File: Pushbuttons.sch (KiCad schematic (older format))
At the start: 19 parts, among them SW1301 Time, SW1302 Date, SW1303 Alarm, SW1304 Display, SW1305 Brightness, SW1306 Select, U1301 MAX6818

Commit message: Resolved an issue with the field names of resistors on anode and grid driver sheets
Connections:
- wire segments 63 -> 82
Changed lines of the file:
@@
 	3240 1770 3240 1810
 Wire Wire Line
-	3240 1770 3880 1770
-Wire Wire Line
-	3560 1730 3560 1810
+	3240 1770 3560 1770
+Wire Wire Line
+	3560 1730 3560 1770
 Wire Wire Line
 	3880 2150 3880 2110
@@
 	3240 2150 3240 2110
 Wire Wire Line
-	3240 2150 3880 2150
-Wire Wire Line
-	3560 2110 3560 2190
+	3240 2150 3560 2150
+Wire Wire Line
+	3560 2110 3560 2150
 Wire Wire Line
 	2460 3390 3970 3390
@@
 ~Encoder_B
 Wire Wire Line
-	4770 3090 7040 3090
-Wire Wire Line
-	4770 3190 7040 3190
-Wire Wire Line
-	4770 3290 7040 3290
-Wire Wire Line
-	4770 3390 7040 3390
-Wire Wire Line
-	4770 3490 7040 3490
-Wire Wire Line
-	4770 3590 7040 3590
-Wire Wire Line
-	4770 3690 7040 3690
-Wire Wire Line
-	4770 3790 7040 3790
+	4770 3090 5540 3090
+Wire Wire Line
+	4770 3190 5720 3190
+Wire Wire Line
+	4770 3290 5900 3290
+Wire Wire Line
+	4770 3390 6080 3390
+Wire Wire Line
+	4770 3490 6260 3490
+Wire Wire Line
+	4770 3590 6440 3590
+Wire Wire Line
+	4770 3690 6620 3690
+Wire Wire Line
+	4770 3790 6800 3790
 $Comp
 L Custom-Library:+3.3V #PWR1313
@@
 	6170 2470 6170 2430
 Wire Wire Line
-	5540 2470 6800 2470
+	5540 2470 5720 2470
 Wire Wire Line
 	6080 2470 6080 2510
@@
 Connection ~ 6800 3790
 NoConn ~ 4770 2940
+Wire Wire Line
+	3560 1770 3880 1770
+Wire Wire Line
+	3560 1770 3560 1810
+Wire Wire Line
+	3560 2150 3880 2150
+Wire Wire Line
+	3560 2150 3560 2190
+Wire Wire Line
+	6080 2470 6170 2470
+Wire Wire Line
+	5900 2470 6080 2470
+Wire Wire Line
+	6170 2470 6260 2470
+Wire Wire Line
+	6260 2470 6440 2470
+Wire Wire Line
+	6440 2470 6620 2470
+Wire Wire Line
+	5720 2470 5900 2470
+Wire Wire Line
+	6620 2470 6800 2470
+Wire Wire Line
+	5540 3090 7040 3090
+Wire Wire Line
+	5720 3190 7040 3190
+Wire Wire Line
+	5900 3290 7040 3290
+Wire Wire Line
+	6080 3390 7040 3390
+Wire Wire Line
+	6260 3490 7040 3490
+Wire Wire Line
+	6440 3590 7040 3590
+Wire Wire Line
+	6620 3690 7040 3690
+Wire Wire Line
+	6800 3790 7040 3790
 $EndSCHEMATC

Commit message: Altered encoder circuit to use little logic to simplify firmware, resized active low signals to it on micro better, updated PDF
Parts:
- removed R1308, R1309: 10k, Resistors_SMD:R_0603, symbol VFD_Clock-rescue:Res_Custom
- added C? (x2): 2.2uF, symbol Custom-Library:C_Custom
- added C? (x2): 0.1uF, Capacitors_SMD:C_0603, symbol Custom-Library:C_Custom
- added R? (x5): 10k, Resistors_SMD:R_0603, symbol VFD_Clock-rescue:Res_Custom
- added R? (x2): 1k, Resistors_SMD:R_0603, symbol Device:R
- added U? (x2): 74LVC2G14, symbol Custom_Library:74LVC2G14_Power
- added U?: 74LVC1G79, symbol Custom_Library:74LVC1G79_Power
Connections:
- net labels added: Encoder_DIR, Encoder_STEP
- net labels removed: ~Encoder_A, ~Encoder_B
- wire segments 82 -> 97

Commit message: Annotated all components, finished assigning footprints, netlist generated
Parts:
- C1304, C1305: renamed from C?; footprint (none) -> Capacitors_SMD:C_0805
- U1302: renamed from U?; footprint (none) -> TO_SOT_Packages_SMD:SOT-363_SC-70-6; Digi-Key PN (none) -> 296-13011-1-ND
- U1303: renamed from U?; footprint (none) -> TO_SOT_Packages_SMD:SOT-353_SC-70-5; Digi-Key PN (none) -> 296-47671-1-ND
- gave numbers to parts that had none: 9
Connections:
- no-connect marks 1 -> 5

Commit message: Switched to QFN micro, various footprint fixes, layed a a few more sheets out, changed puchbutton debouncers
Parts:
- removed C1301: 1nF, Capacitors_SMD:C_0603, symbol Custom-Library:C_Custom
- removed R1307: 10k, Resistors_SMD:R_0603, symbol VFD_Clock-rescue:Res_Custom
- removed U1301: MAX6818, Housings_SSOP:SSOP-20_5.3x7.2mm_Pitch0.65mm, symbol Custom-Library:MAX6818
- added C1303, C1308, C1309, C1310: 0.1uF, Capacitors_SMD:C_0603, symbol Custom-Library:C_Custom
- added U1301, U1304, U1305, U1306, U1307, U1308: MAX6816, TO_SOT_Packages_SMD:SOT-143, symbol Custom_Library:MAX6816
- C1302: value 10nF -> 0.1uF
- R1301, R1302, R1303, R1304, R1305, R1306: Wattage 1/16W -> 1/10W; display_footprint 0402 -> 0603
- renumbered C1303 to C1301
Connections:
- wire segments 97 -> 53
- no-connect marks 5 -> 0

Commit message: Added a bunch of Digi-Key PN's
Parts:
- C1301, C1302, C1303, C1306, C1307, C1308, C1309, C1310: Digi-Key PN (none) -> 399-6856-1-ND
- R1301, R1302, R1303, R1304, R1305, R1306, R1312, R1313, R1314: Digi-Key PN (none) -> 541-10.0KHCT-ND
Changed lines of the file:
@@
 F 5 "50V" H 2540 1730 50  0000 R CNN "Voltage"
 F 6 "X7R" H 2540 1630 50  0000 R CNN "Dielectric"
+F 7 "399-6856-1-ND" H 0   0   50  0001 C CNN "Digi-Key PN"
 	1    2690 1730
 	-1   0    0    -1
@@
 F 5 "1/10W" V 3160 5440 50  0001 C CNN "Wattage"
 F 6 "0603" V 3080 5440 50  0001 C CNN "display_footprint"
+F 7 "" H 0   0   50  0001 C CNN "Digi-Key PN"
 	1    3260 5440
 	0    -1   -1   0
@@
 F 5 "1/10W" V 3160 5640 50  0001 C CNN "Wattage"
 F 6 "0603" V 3080 5640 50  0001 C CNN "display_footprint"
+F 7 "" H 0   0   50  0001 C CNN "Digi-Key PN"
 	1    3260 5640
 	0    -1   -1   0
@@
 F 5 "50V" H 5300 6360 50  0000 R CNN "Voltage"
 F 6 "X7R" H 5300 6260 50  0000 R CNN "Dielectric"
+F 7 "399-6856-1-ND" H 0   0   50  0001 C CNN "Digi-Key PN"
 	1    5450 6360
 	-1   0    0    -1
@@
 F 5 "1%" H 6740 6130 50  0000 L CNN "Tolerance"
 F 6 "1/10W" H 6730 6200 50  0000 L CNN "Wattage"
+F 7 "541-10.0KHCT-ND" H 0   0   50  0001 C CNN "Digi-Key PN"
 	1    6670 6150
 	-1   0    0    -1
@@
 F 5 "1%" H 7370 6130 50  0000 L CNN "Tolerance"
 F 6 "1/10W" H 7360 6200 50  0000 L CNN "Wattage"
+F 7 "541-10.0KHCT-ND" H 0   0   50  0001 C CNN "Digi-Key PN"
 	1    7300 6150
 	-1   0    0    -1
@@
 F 5 "50V" H 7910 6330 50  0000 R CNN "Voltage"
 F 6 "X7R" H 7910 6230 50  0000 R CNN "Dielectric"
+F 7 "399-6856-1-ND" H 0   0   50  0001 C CNN "Digi-Key PN"
 	1    8060 6330
 	-1   0    0    -1
@@
 F 5 "1%" H 9360 5830 50  0000 L CNN "Tolerance"
 F 6 "1/10W" H 9350 5900 50  0000 L CNN "Wattage"
+F 7 "541-10.0KHCT-ND" H 0   0   50  0001 C CNN "Digi-Key PN"
 	1    9290 5850
 	-1   0    0    -1
@@
 F 5 "1%" H 3950 1050 50  0000 L CNN "Tolerance"
 F 6 "1/10W" H 3940 1120 50  0000 L CNN "Wattage"
+F 7 "541-10.0KHCT-ND" H 0   0   50  0001 C CNN "Digi-Key PN"
 	1    3880 1070
 	1    0    0    -1
@@
 F 5 "50V" H 5540 1730 50  0000 R CNN "Voltage"
 F 6 "X7R" H 5540 1630 50  0000 R CNN "Dielectric"
+F 7 "399-6856-1-ND" H 0   0   50  0001 C CNN "Digi-Key PN"
 	1    5690 1730
 	-1   0    0    -1
@@
 F 5 "1%" H 6950 1050 50  0000 L CNN "Tolerance"
 F 6 "1/10W" H 6940 1120 50  0000 L CNN "Wattage"
+F 7 "541-10.0KHCT-ND" H 0   0   50  0001 C CNN "Digi-Key PN"
 	1    6880 1070
 	1    0    0    -1
@@
 F 5 "50V" H 2540 2980 50  0000 R CNN "Voltage"
 F 6 "X7R" H 2540 2880 50  0000 R CNN "Dielectric"
+F 7 "399-6856-1-ND" H 0   0   50  0001 C CNN "Digi-Key PN"
 	1    2690 2980
 	-1   0    0    -1
@@
 F 5 "1%" H 3950 2300 50  0000 L CNN "Tolerance"
 F 6 "1/10W" H 3940 2370 50  0000 L CNN "Wattage"
+F 7 "541-10.0KHCT-ND" H 0   0   50  0001 C CNN "Digi-Key PN"
 	1    3880 2320
 	1    0    0    -1
@@
 F 5 "50V" H 5540 2980 50  0000 R CNN "Voltage"
 F 6 "X7R" H 5540 2880 50  0000 R CNN "Dielectric"
+F 7 "399-6856-1-ND" H 0   0   50  0001 C CNN "Digi-Key PN"
 	1    5690 2980
 	-1   0    0    -1
@@
 F 5 "1%" H 6950 2300 50  0000 L CNN "Tolerance"
 F 6 "1/10W" H 6940 2370 50  0000 L CNN "Wattage"
+F 7 "541-10.0KHCT-ND" H 0   0   50  0001 C CNN "Digi-Key PN"
 	1    6880 2320
 	1    0    0    -1
@@
 F 5 "50V" H 2540 4230 50  0000 R CNN "Voltage"
 F 6 "X7R" H 2540 4130 50  0000 R CNN "Dielectric"
+F 7 "399-6856-1-ND" H 0   0   50  0001 C CNN "Digi-Key PN"
 	1    2690 4230
 	-1   0    0    -1
@@
 F 5 "1%" H 3950 3550 50  0000 L CNN "Tolerance"
 F 6 "1/10W" H 3940 3620 50  0000 L CNN "Wattage"
+F 7 "541-10.0KHCT-ND" H 0   0   50  0001 C CNN "Digi-Key PN"
 	1    3880 3570
 	1    0    0    -1
@@
 F 5 "50V" H 5540 4230 50  0000 R CNN "Voltage"
 F 6 "X7R" H 5540 4130 50  0000 R CNN "Dielectric"
+F 7 "399-6856-1-ND" H 0   0   50  0001 C CNN "Digi-Key PN"
 	1    5690 4230
 	-1   0    0    -1
@@
 F 5 "1%" H 6950 3550 50  0000 L CNN "Tolerance"
 F 6 "1/10W" H 6940 3620 50  0000 L CNN "Wattage"
+F 7 "541-10.0KHCT-ND" H 0   0   50  0001 C CNN "Digi-Key PN"
 	1    6880 3570
 	1    0    0    -1

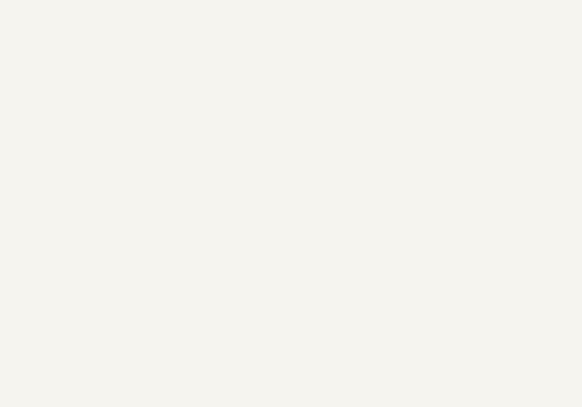
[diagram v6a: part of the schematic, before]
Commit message: Arranged more components on PCB, cleaned up schematic, added page titles, finished finding DigiKey PN's
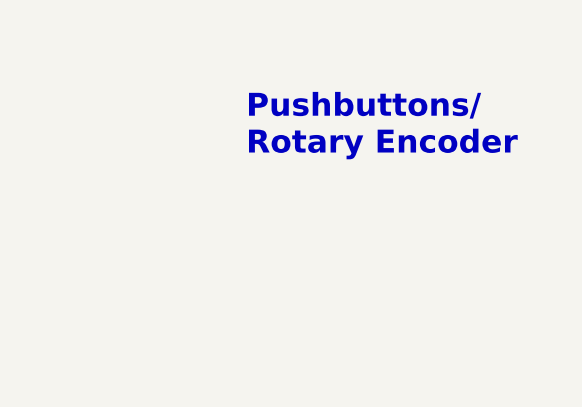
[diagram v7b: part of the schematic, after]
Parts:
- R1301, R1302, R1303, R1304, R1305, R1306, R1312, R1313, R1314: Digi-Key PN 541-10.0KHCT-ND -> P10.0KHCT-ND
- R1308, R1309: Digi-Key PN (none) -> P10.0KHCT-ND; Wattage 1/16W -> 1/10W; display_footprint 0402 -> 0603
- R1310, R1311: Digi-Key PN (none) -> RMCF0603FT1K00CT-ND
- SW1301, SW1302, SW1303, SW1304, SW1305: Digi-Key PN (none) -> 450-1650-ND
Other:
- note added: "Pushbuttons/\nRotary Encoder"
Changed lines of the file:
@@
 F 2 "Buttons_Switches_THT:SW_PUSH_6mm" H 2520 1470 50  0001 C CNN
 F 3 "" H 2520 1470 50  0001 C CNN
+F 4 "450-1650-ND" H 0   0   50  0001 C CNN "Digi-Key PN"
 	1    2520 1270
 	1    0    0    -1
@@
 F 2 "Buttons_Switches_THT:SW_PUSH_6mm" H 5520 1470 50  0001 C CNN
 F 3 "" H 5520 1470 50  0001 C CNN
+F 4 "450-1650-ND" H 0   0   50  0001 C CNN "Digi-Key PN"
 	1    5520 1270
 	1    0    0    -1
@@
 F 2 "Buttons_Switches_THT:SW_PUSH_6mm" H 2520 2720 50  0001 C CNN
 F 3 "" H 2520 2720 50  0001 C CNN
+F 4 "450-1650-ND" H 0   0   50  0001 C CNN "Digi-Key PN"
 	1    2520 2520
 	1    0    0    -1
@@
 F 2 "Buttons_Switches_THT:SW_PUSH_6mm" H 5520 2720 50  0001 C CNN
 F 3 "" H 5520 2720 50  0001 C CNN
+F 4 "450-1650-ND" H 0   0   50  0001 C CNN "Digi-Key PN"
 	1    5520 2520
 	1    0    0    -1
@@
 F 2 "Buttons_Switches_THT:SW_PUSH_6mm" H 5520 3970 50  0001 C CNN
 F 3 "" H 5520 3970 50  0001 C CNN
+F 4 "450-1650-ND" H 0   0   50  0001 C CNN "Digi-Key PN"
 	1    5520 3770
 	1    0    0    -1
@@
 F 2 "Resistors_SMD:R_0603" H 2660 5110 50  0001 C CNN
 F 3 "" H 2660 5110 50  0001 C CNN
-F 4 "0402" V 2760 5110 50  0001 C CNN "display_footprint"
+F 4 "0603" V 2760 5110 50  0001 C CNN "display_footprint"
 F 5 "1%" V 2860 5110 50  0001 C CNN "Tolerance"
-F 6 "1/16W" V 2960 5110 50  0001 C CNN "Wattage"
+F 6 "1/10W" V 2960 5110 50  0001 C CNN "Wattage"
+F 7 "P10.0KHCT-ND" H 0   0   50  0001 C CNN "Digi-Key PN"
 	1    2660 5110
 	1    0    0    -1
@@
 F 2 "Resistors_SMD:R_0603" H 2840 5110 50  0001 C CNN
 F 3 "" H 2840 5110 50  0001 C CNN
-F 4 "0402" V 2940 5110 50  0001 C CNN "display_footprint"
+F 4 "0603" V 2940 5110 50  0001 C CNN "display_footprint"
 F 5 "1%" V 3040 5110 50  0001 C CNN "Tolerance"
-F 6 "1/16W" V 3140 5110 50  0001 C CNN "Wattage"
+F 6 "1/10W" V 3140 5110 50  0001 C CNN "Wattage"
+F 7 "P10.0KHCT-ND" H 0   0   50  0001 C CNN "Digi-Key PN"
 	1    2840 5110
 	1    0    0    -1
@@
 F 5 "1/10W" V 3160 5440 50  0001 C CNN "Wattage"
 F 6 "0603" V 3080 5440 50  0001 C CNN "display_footprint"
-F 7 "" H 0   0   50  0001 C CNN "Digi-Key PN"
+F 7 "RMCF0603FT1K00CT-ND" H 0   0   50  0001 C CNN "Digi-Key PN"
 	1    3260 5440
 	0    -1   -1   0
@@
 F 5 "1/10W" V 3160 5640 50  0001 C CNN "Wattage"
 F 6 "0603" V 3080 5640 50  0001 C CNN "display_footprint"
-F 7 "" H 0   0   50  0001 C CNN "Digi-Key PN"
+F 7 "RMCF0603FT1K00CT-ND" H 0   0   50  0001 C CNN "Digi-Key PN"
 	1    3260 5640
 	0    -1   -1   0
@@
 U 1 1 5B56624B
 P 8280 5630
-F 0 "U1303" H 8180 5830 50  0000 R CNN
+F 0 "U1303" H 8410 5830 50  0000 L CNN
 F 1 "74LVC1G79" H 8620 5400 50  0000 C CNN
 F 2 "TO_SOT_Packages_SMD:SOT-353_SC-70-5" H 8280 5630 50  0001 C CNN
@@
 F 5 "1%" H 6740 6130 50  0000 L CNN "Tolerance"
 F 6 "1/10W" H 6730 6200 50  0000 L CNN "Wattage"
-F 7 "541-10.0KHCT-ND" H 0   0   50  0001 C CNN "Digi-Key PN"
+F 7 "P10.0KHCT-ND" H 0   0   50  0001 C CNN "Digi-Key PN"
 	1    6670 6150
 	-1   0    0    -1
@@
 F 5 "1%" H 7370 6130 50  0000 L CNN "Tolerance"
 F 6 "1/10W" H 7360 6200 50  0000 L CNN "Wattage"
-F 7 "541-10.0KHCT-ND" H 0   0   50  0001 C CNN "Digi-Key PN"
+F 7 "P10.0KHCT-ND" H 0   0   50  0001 C CNN "Digi-Key PN"
 	1    7300 6150
 	-1   0    0    -1
@@
 F 5 "1%" H 9360 5830 50  0000 L CNN "Tolerance"
 F 6 "1/10W" H 9350 5900 50  0000 L CNN "Wattage"
-F 7 "541-10.0KHCT-ND" H 0   0   50  0001 C CNN "Digi-Key PN"
+F 7 "P10.0KHCT-ND" H 0   0   50  0001 C CNN "Digi-Key PN"
 	1    9290 5850
 	-1   0    0    -1
@@
 F 5 "1%" H 3950 1050 50  0000 L CNN "Tolerance"
 F 6 "1/10W" H 3940 1120 50  0000 L CNN "Wattage"
-F 7 "541-10.0KHCT-ND" H 0   0   50  0001 C CNN "Digi-Key PN"
+F 7 "P10.0KHCT-ND" H 0   0   50  0001 C CNN "Digi-Key PN"
 	1    3880 1070
 	1    0    0    -1
@@
 F 5 "1%" H 6950 1050 50  0000 L CNN "Tolerance"
 F 6 "1/10W" H 6940 1120 50  0000 L CNN "Wattage"
-F 7 "541-10.0KHCT-ND" H 0   0   50  0001 C CNN "Digi-Key PN"
+F 7 "P10.0KHCT-ND" H 0   0   50  0001 C CNN "Digi-Key PN"
 	1    6880 1070
 	1    0    0    -1
@@
 F 5 "1%" H 3950 2300 50  0000 L CNN "Tolerance"
 F 6 "1/10W" H 3940 2370 50  0000 L CNN "Wattage"
-F 7 "541-10.0KHCT-ND" H 0   0   50  0001 C CNN "Digi-Key PN"
+F 7 "P10.0KHCT-ND" H 0   0   50  0001 C CNN "Digi-Key PN"
 	1    3880 2320
 	1    0    0    -1
@@
 F 5 "1%" H 6950 2300 50  0000 L CNN "Tolerance"
 F 6 "1/10W" H 6940 2370 50  0000 L CNN "Wattage"
-F 7 "541-10.0KHCT-ND" H 0   0   50  0001 C CNN "Digi-Key PN"
+F 7 "P10.0KHCT-ND" H 0   0   50  0001 C CNN "Digi-Key PN"
 	1    6880 2320
 	1    0    0    -1
@@
 F 5 "1%" H 3950 3550 50  0000 L CNN "Tolerance"
 F 6 "1/10W" H 3940 3620 50  0000 L CNN "Wattage"
-F 7 "541-10.0KHCT-ND" H 0   0   50  0001 C CNN "Digi-Key PN"
+F 7 "P10.0KHCT-ND" H 0   0   50  0001 C CNN "Digi-Key PN"
 	1    3880 3570
 	1    0    0    -1
@@
 F 5 "1%" H 6950 3550 50  0000 L CNN "Tolerance"
 F 6 "1/10W" H 6940 3620 50  0000 L CNN "Wattage"
-F 7 "541-10.0KHCT-ND" H 0   0   50  0001 C CNN "Digi-Key PN"
+F 7 "P10.0KHCT-ND" H 0   0   50  0001 C CNN "Digi-Key PN"
 	1    6880 3570
 	1    0    0    -1
@@
 	7520 3770 6880 3770
 Connection ~ 6880 3770
+Text Notes 9010 1090 0    100  ~ 20
+Pushbuttons/\nRotary Encoder
 $EndSCHEMATC

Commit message: Placed VAN power supply and asociated circuits
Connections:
- wire segments 53 -> 54
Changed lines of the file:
@@
 L power:GND #PWR01301
 U 1 1 5A4D2A4C
-P 1910 5640
-F 0 "#PWR01301" H 1910 5390 50  0001 C CNN
-F 1 "GND" H 1910 5490 50  0000 C CNN
-F 2 "" H 1910 5640 50  0001 C CNN
-F 3 "" H 1910 5640 50  0001 C CNN
-	1    1910 5640
+P 1800 5440
+F 0 "#PWR01301" H 1800 5190 50  0001 C CNN
+F 1 "GND" H 1800 5290 50  0000 C CNN
+F 2 "" H 1800 5440 50  0001 C CNN
+F 3 "" H 1800 5440 50  0001 C CNN
+	1    1800 5440
 	0    1    1    0
 $EndComp
@@
 Text GLabel 4290 3770 2    60   Output ~ 0
 ~Encoder_PB
-Wire Wire Line
-	1910 5440 1870 5440
 $Comp
 L VFD_Clock-rescue:Res_Custom R1308
@@
 $EndComp
 Wire Wire Line
-	1870 5440 1870 3770
-Wire Wire Line
 	1870 3770 2720 3770
 Wire Wire Line
@@
 Text Notes 9010 1090 0    100  ~ 20
 Pushbuttons/\nRotary Encoder
+Wire Wire Line
+	1870 5640 1910 5640
+Wire Wire Line
+	1870 3770 1870 5640
+Wire Wire Line
+	1800 5440 1910 5440
 $EndSCHEMATC
